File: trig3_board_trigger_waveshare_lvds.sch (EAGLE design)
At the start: 86 parts, among them IC1 SN65LVDT388ADBT, IC2 SN65LVDT388ADBT, IC3 SN65LVDT388ADBT, IC4 SN65LVDT388ADBT, IC5 SN65LVDT388ADBT, IC6 SN65LVDT388ADBT, IC7 SN65LVDT388ADBT, IC8 SN65LVDT388ADBT, J12 4p-2.54, J19 6HE-160-VG64AC, J20 8pin, J3 4p-2.54, J4 4p-2.54, X1 87758-1616, X13 87758-2816, X14 87758-2816, X15 87758-1616, X16 87758-1616, X17 87758-2816, X18 87758-2816, X2 87758-1616

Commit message: better
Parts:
- added IN65, IN66, IN67, IN68, IN69, IN70, IN71, IN72, IN73, IN74, IN75, IN76, IN77, IN78, IN79, IN80, OUT17, OUT18, OUT19, OUT20, OUT21, OUT22, OUT23, OUT24, OUT25, OUT26, OUT27, OUT28, OUT29, OUT30, OUT31, OUT32: BU-SMB-V, con-coax:BU-SMB-V
- added J1, J10, J11, J13, J14, J15, J16, J17, J2, J5, J6, J7, J8, J9: 8pin, SparkFun-Connectors:CONN_08"
- LED_OE: value Red -> OutputEn
- renumbered 145OUT16 to OUT16, 147OUT15 to OUT15, 159OUT14 to OUT14, 161OUT13 to OUT13, 164OUT12 to OUT12, 167OUT11 to OUT11, 169OUT10 to OUT10, 173OUT9 to OUT9, 174OUT1 to OUT1, 175OUT5 to OUT5, 176OUT2 to OUT2, 177OUT6 to OUT6, 181OUT3 to OUT3, 182OUT7 to OUT7, 183OUT4 to OUT4, 184OUT8 to OUT8, LED1 to LED_OE
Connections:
- removed net IO145_IN4: VSLUE4.2A3, VSLUE4.2A4, X13-28.S
- removed net IO147_IN3: VSLUE4.2A1, VSLUE4.2A2, X13-26.S
- removed net IO159_IN2: VSLUE4.1A3, VSLUE4.1A4, X13-22.S
- removed net IO161_IN1: VSLUE4.1A1, VSLUE4.1A2, X13-20.S
- removed net IO164_IN4: VSLUE3.2A3, VSLUE3.2A4, X13-18.S
- removed net IO167_IN3: VSLUE3.2A1, VSLUE3.2A2, X13-16.S
- removed net IO169_IN2: VSLUE3.1A3, VSLUE3.1A4, X13-14.S
- removed net IO173_IN1: VSLUE3.1A1, VSLUE3.1A2, X13-12.S
- removed net IO174_IN1: VSLUE.1A1, VSLUE.1A2, X13-9.S
- removed net IO175_IN1: VSLUE2.1A1, VSLUE2.1A2, X13-10.S
- removed net IO176_IN2: VSLUE.1A3, VSLUE.1A4, X13-7.S
- removed net IO177_IN2: VSLUE2.1A3, VSLUE2.1A4, X13-8.S
- removed net IO181_IN3: VSLUE.2A1, VSLUE.2A2, X13-5.S
- removed net IO182_IN3: VSLUE2.2A1, VSLUE2.2A2, X13-6.S
- removed net IO183_IN4: VSLUE.2A3, VSLUE.2A4, X13-3.S
- removed net IO184_IN4: VSLUE2.2A3, VSLUE2.2A4, X13-4.S
- removed net N$130: X17-25.S
- removed net N$155: X17-26.S
- removed net N$182: X14-25.S
- removed net N$183: X14-23.S
- removed net N$184: X14-21.S
- removed net N$185: X14-19.S
- removed net N$186: X14-17.S
- removed net N$187: X14-15.S
- removed net N$188: X14-13.S
- removed net N$189: X14-11.S
- removed net N$190: X14-9.S
- removed net N$191: X14-7.S
- removed net N$192: X14-5.S
- removed net N$193: X14-3.S
- removed net N$194: X14-1.S
- removed net N$195: X14-26.S
- removed net N$196: X14-24.S
- removed net N$197: X14-22.S
- removed net N$198: X14-20.S
- removed net N$199: X14-18.S
- removed net N$200: X14-16.S
- removed net N$201: X14-14.S
- removed net N$202: X14-12.S
- removed net N$203: X14-10.S
- removed net N$204: X14-8.S
- removed net N$205: X14-6.S
- removed net N$206: X14-4.S
- removed net N$207: X14-2.S
- removed net N$217: X16-1.S
- removed net N$218: X16-3.S
- removed net N$219: X16-5.S
- removed net N$220: X16-7.S
- removed net N$221: X16-9.S
- removed net N$222: X16-11.S
- removed net N$223: X16-13.S
- removed net N$224: X16-15.S
- removed net N$225: X15-1.S
- removed net N$226: X15-3.S
- removed net N$227: X15-5.S
- removed net N$228: X15-7.S
- removed net N$229: X15-9.S
- removed net N$230: X15-11.S
- removed net N$231: X15-13.S
- removed net N$232: X15-15.S
- removed net N$249: X1-2.S
- removed net N$250: X1-4.S
- removed net N$251: X1-6.S
- removed net N$252: X1-8.S
- new net IN65: IN65.1, J7.8, X16-1.S
- new net IN66: IN66.1, J7.7, X16-3.S
- new net IN67: IN67.1, J7.6, X16-5.S
- new net IN68: IN68.1, J7.5, X16-7.S
- new net IN69: IN69.1, J7.4, X16-9.S
- new net IN70: IN70.1, J7.3, X16-11.S
- new net IN71: IN71.1, J7.2, X16-13.S
- new net IN72: IN72.1, J7.1, X16-15.S
- new net IN73: IN73.1, J8.8, X15-1.S
- new net IN74: IN74.1, J8.7, X15-3.S
- new net IN75: IN75.1, J8.6, X15-5.S
- new net IN76: IN76.1, J8.5, X15-7.S
- new net IN77: IN77.1, J8.4, X15-9.S
- new net IN78: IN78.1, J8.3, X15-11.S
- new net IN79: IN79.1, J8.2, X15-13.S
- new net IN80: IN80.1, J8.1, X15-15.S
- new net IO10: J14.6, X14-5.S
- new net IO11: J14.5, X14-7.S
- new net IO12: J14.4, X14-9.S
- new net IO13: J14.3, X14-11.S
- new net IO14: J14.2, X14-13.S
- new net IO15: J14.1, X14-15.S
- new net IO16: J15.8, X14-2.S
- new net IO17: J15.7, X14-4.S
- new net IO18: J15.6, X14-6.S
- new net IO19: J15.5, X14-8.S
- new net IO20: J15.4, X14-10.S
- new net IO21: J15.3, X14-12.S
- new net IO22: J15.2, X14-14.S
- new net IO23: J15.1, X14-16.S
- new net IO8: J14.8, X14-1.S
- new net IO9: J14.7, X14-3.S
- new net OUT10IN: J2.4, VSLUE3.1A3, VSLUE3.1A4, X13-14.S
- new net OUT11IN: J2.6, VSLUE3.2A1, VSLUE3.2A2, X13-16.S
- new net OUT12IN: J2.8, VSLUE3.2A3, VSLUE3.2A4, X13-18.S
- new net OUT13IN: J5.2, VSLUE4.1A1, VSLUE4.1A2, X13-20.S
- new net OUT14IN: J5.4, VSLUE4.1A3, VSLUE4.1A4, X13-22.S
- new net OUT15IN: J5.6, VSLUE4.2A1, VSLUE4.2A2, X13-26.S
- new net OUT16IN: J5.8, VSLUE4.2A3, VSLUE4.2A4, X13-28.S
- new net OUT17: J17.1, OUT17.1, X17-25.S
- new net OUT18: J17.2, OUT18.1, X17-26.S
- new net OUT19: J17.3, OUT19.1, X14-17.S
- new net OUT1IN: J1.2, VSLUE.1A1, VSLUE.1A2, X13-9.S
- new net OUT20: J17.4, OUT20.1, X14-19.S
- new net OUT21: J17.5, OUT21.1, X14-21.S
- new net OUT22: J17.6, OUT22.1, X14-23.S
- new net OUT23: J17.7, OUT23.1, X14-25.S
- new net OUT24: J17.8, OUT24.1, X14-18.S
- new net OUT25: J16.1, OUT25.1, X14-20.S
- new net OUT26: J16.2, OUT26.1, X14-22.S
- new net OUT27: J16.3, OUT27.1, X14-24.S
- new net OUT28: J16.4, OUT28.1, X14-26.S
- new net OUT29: J16.5, J9.8, OUT29.1, X1-2.S, X17-27.S
- new net OUT2IN: J1.4, VSLUE.1A3, VSLUE.1A4, X13-7.S
- new net OUT30: J16.6, J9.7, OUT30.1, X1-4.S, X17-28.S
- new net OUT31: J16.7, J9.6, OUT31.1, X1-6.S, X14-27.S
- new net OUT32: J16.8, J9.5, OUT32.1, X1-8.S, X14-28.S
- new net OUT3IN: J1.6, VSLUE.2A1, VSLUE.2A2, X13-5.S
- new net OUT4IN: J1.8, VSLUE.2A3, VSLUE.2A4, X13-3.S
- new net OUT5IN: J6.2, VSLUE2.1A1, VSLUE2.1A2, X13-10.S
- new net OUT6IN: J6.4, VSLUE2.1A3, VSLUE2.1A4, X13-8.S
- new net OUT7IN: J6.6, VSLUE2.2A1, VSLUE2.2A2, X13-6.S
- new net OUT8IN: J6.8, VSLUE2.2A3, VSLUE2.2A4, X13-4.S
- new net OUT9IN: J2.2, VSLUE3.1A1, VSLUE3.1A2, X13-12.S
- net GND: now also IN65.2, IN66.2, IN67.2, IN68.2, IN69.2, IN70.2, IN71.2, IN72.2, IN73.2, IN74.2, IN75.2, IN76.2, IN77.2, IN78.2, IN79.2, IN80.2, J1.1, J1.3, J1.5, J1.7, J2.1, J2.3, J2.5, J2.7, J5.1, J5.3, J5.5, J5.7, J6.1, J6.3, J6.5, J6.7, OUT17.2, OUT18.2, OUT19.2, OUT20.2, OUT21.2, OUT22.2, OUT23.2, OUT24.2, OUT25.2, OUT26.2, OUT27.2, OUT28.2, OUT29.2, OUT30.2, OUT31.2, OUT32.2
- net N$253: now also J9.4
- net N$254: now also J9.3
- net N$255: now also J9.2
- net N$256: now also J9.1
- net N$257: now also J10.8
- net N$258: now also J10.7
- net N$259: now also J10.6
- net N$260: now also J10.5
- net N$261: now also J10.4
- net N$262: now also J10.3
- net N$263: now also J10.2
- net N$264: now also J10.1
- net N$265: now also J11.8
- net N$266: now also J11.7
- net N$267: now also J11.6
- net N$268: now also J11.5
- net N$269: now also J11.4
- net N$270: now also J11.3
- net N$271: now also J11.2
- net N$272: now also J11.1
- net N$273: now also J13.8
- net N$274: now also J13.7
- net N$275: now also J13.6
- net N$276: now also J13.5
- net N$277: now also J13.4
- net N$278: now also J13.3
- net N$279: now also J13.2
- net N$280: now also J13.1

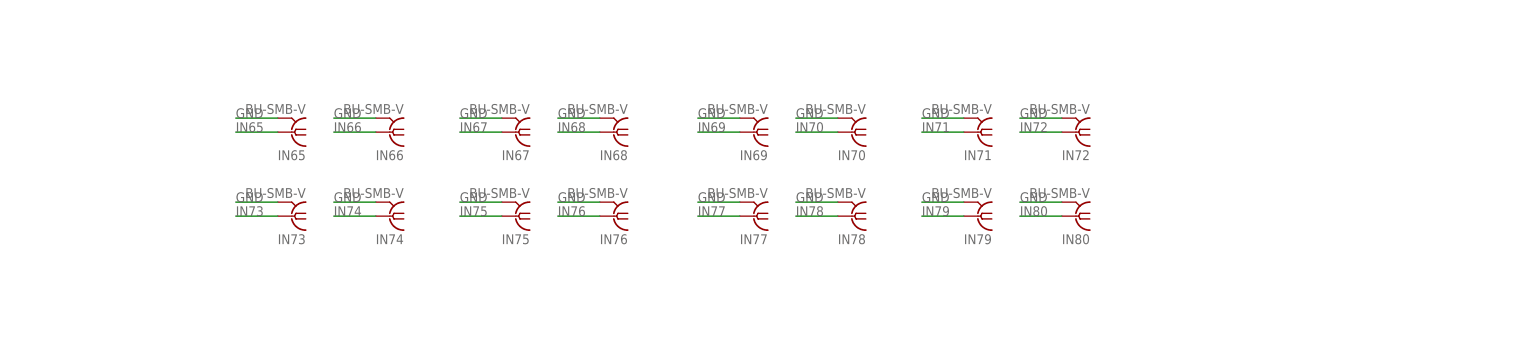
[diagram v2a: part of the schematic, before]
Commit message: added 50 ohm term on extra sma inputs, v1.44
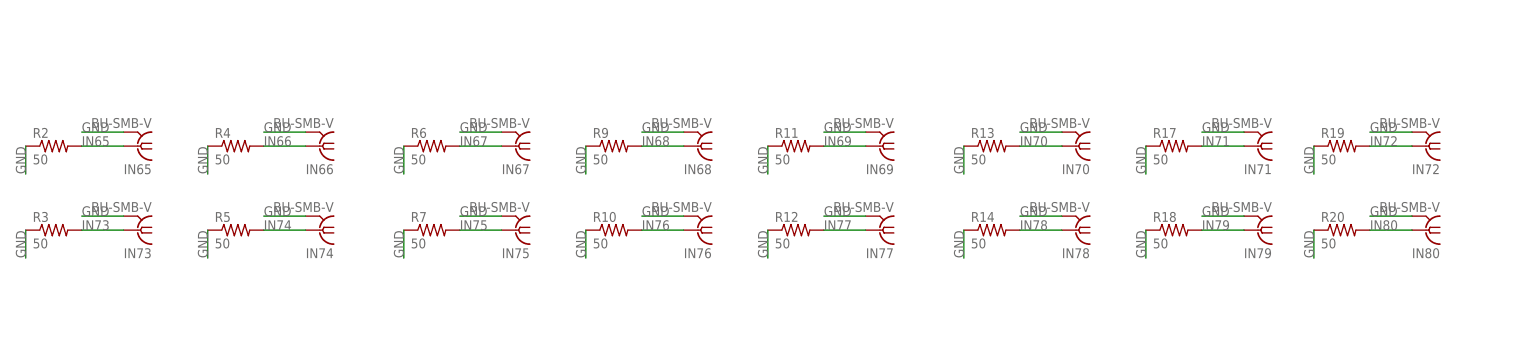
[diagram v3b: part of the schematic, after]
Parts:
- added R10, R11, R12, R13, R14, R17, R18, R19, R2, R20, R3, R4, R5, R6, R7, R9: 50, SparkFun-Resistors:RESISTORAXIAL-0.3
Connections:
- net GND: now also R10.1, R11.1, R12.1, R13.1, R14.1, R17.1, R18.1, R19.1, R2.1, R20.1, R3.1, R4.1, R5.1, R6.1, R7.1, R9.1
- net IN65: now also R2.2
- net IN66: now also R4.2
- net IN67: now also R6.2
- net IN68: now also R9.2
- net IN69: now also R11.2
- net IN70: now also R13.2
- net IN71: now also R17.2
- net IN72: now also R19.2
- net IN73: now also R3.2
- net IN74: now also R5.2
- net IN75: now also R7.2
- net IN76: now also R10.2
- net IN77: now also R12.2
- net IN78: now also R14.2
- net IN79: now also R18.2
- net IN80: now also R20.2
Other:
- moved on the sheet: IN65, IN66, IN67, IN68, IN69, IN70, IN71, IN72, IN73, IN74, IN75, IN76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
